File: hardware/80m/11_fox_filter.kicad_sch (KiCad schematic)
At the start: 22 parts, among them J502 FOX ONLY / compact

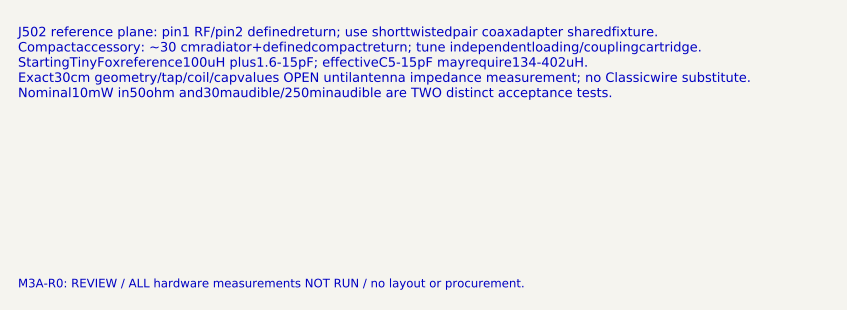
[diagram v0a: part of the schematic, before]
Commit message: Correct RF80 timer polarities and arming logic for M3A-R1 review
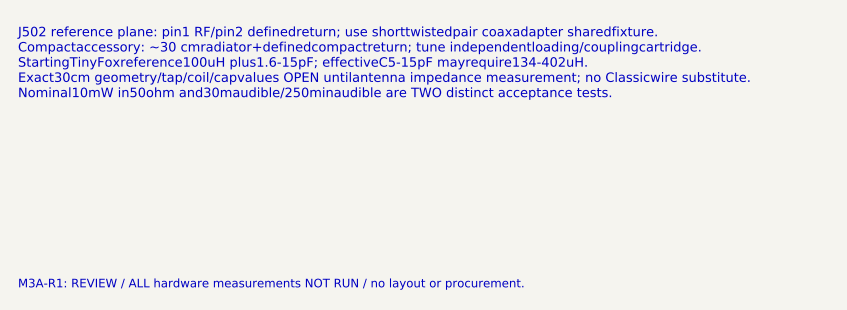
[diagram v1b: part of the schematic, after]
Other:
- note added: "M3A-R1: REVIEW / ALL hardware measurements NOT RUN / no layout or procurement."
- note removed: "M3A-R0: REVIEW / ALL hardware measurements NOT RUN / no layout or procurement."

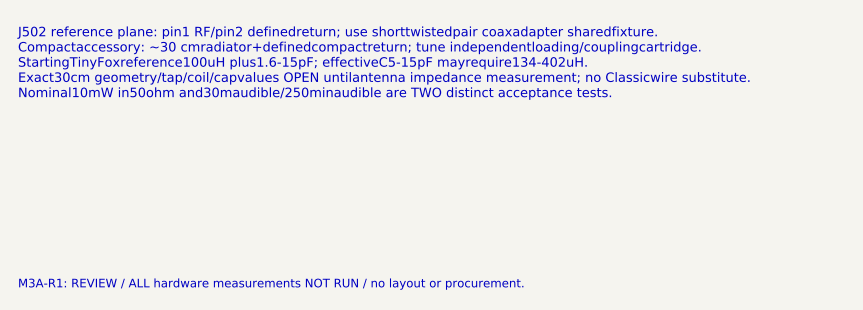
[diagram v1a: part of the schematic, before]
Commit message: Preserve M3B-E1 evaluation PCB before independent-review corrections
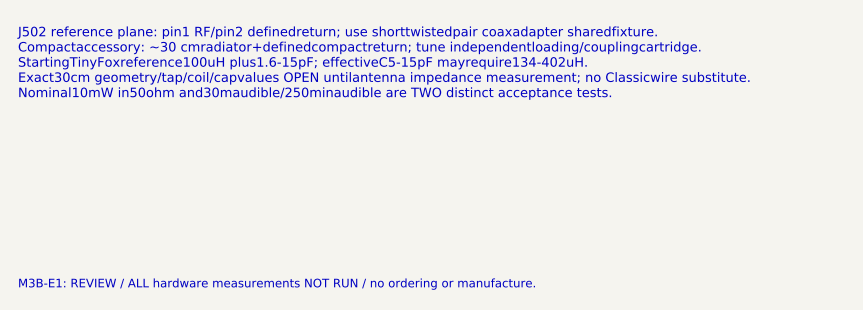
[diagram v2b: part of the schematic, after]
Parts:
- R516: Engineering_Note Absent=high enables normalwhenrequested. Presentlow inhibitsnormalregardlessfirmware; Disarmbeforeplugchanges; JSTXHdoesnotguaranteesequentialmating. Dated M2 distributor observation; no fresh basket verification. -> Absent=high enables normalwhenrequested. Presentlow inhibitsnormalregardlessfirmware; Disarmbeforeplugchanges; JSTXHdoesnotguaranteesequentialmating.
- TP510, TP511, TP512, TP513: now left out of the parts list
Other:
- note added: "M3B-E1: REVIEW / ALL hardware measurements NOT RUN / no ordering or manufacture."
- note removed: "M3A-R1: REVIEW / ALL hardware measurements NOT RUN / no layout or procurement."

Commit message: Correct RF80 M3B-E2 physical pinouts and audit manufacturing readiness
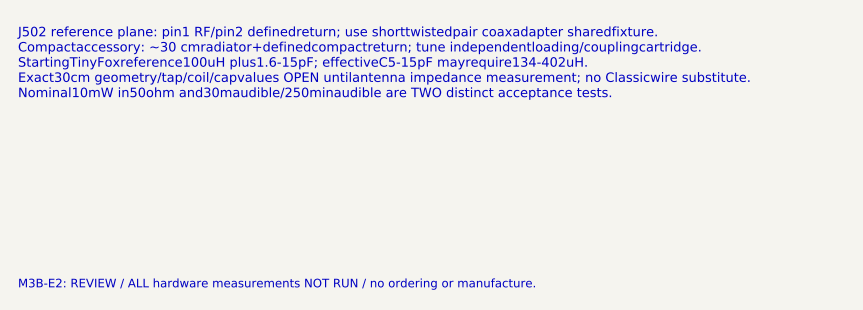
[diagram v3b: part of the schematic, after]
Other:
- note added: "M3B-E2: REVIEW / ALL hardware measurements NOT RUN / no ordering or manufacture."
- note removed: "M3B-E1: REVIEW / ALL hardware measurements NOT RUN / no ordering or manufacture."
